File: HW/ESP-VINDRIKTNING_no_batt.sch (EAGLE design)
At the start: 47 parts, among them IC1 PI4ULS5V202UEX, IC3 CH340C, J1 USB-C_DONLY918-418K2022Y40000, Q1 MMDT3904, Q6 DMG2305UX, U1 ESP-12S

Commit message: new
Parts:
- removed D1: 1N5819WS, diode:DIODE-SOD323-R
- removed SLEEP: JUMPER-SMT_2_NO_NO-SILK, LasKKit-Connectors:JUMPER-SMT_2_NO_NO-SILK
- removed U1: ESP-12S, LasKKit-Modules:WIFI_ESP12SMD
- added C6: 100nF, rcl:C-EUC0603
- added C7: 47uF, rcl:C-EUC0603
- added ESP32: ESP32-WROOM-32D, LasKKit-Modules:ESP32-WROOM-32D
- added Q2, Q3, Q4, Q5: AO3404A, SparkFun-DiscreteSemi:MOSFET-NCH-AO3404A
- added R10, R7: 100k, rcl:R-EU_R0402
- added R6: 10k, rcl:R-EU_R0402
- C1: value 100nF -> 20p; device rcl:C-EUC0603 -> rcl:C-EUC0402
- C2: value 10uF -> 20p; device rcl:C-EUC0603 -> rcl:C-EUC0402
- I2C: value JST-XH-4 -> JST-PH-4; device LasKKit-Connectors:JST-XH-4 -> LasKKit-Connectors:JST-PH-4; LCSC_PART (none) -> C2321
- Q6: value DMG2305UX -> 12MHz; device transistor-power:FDN360P -> crystal-geyer_V1_0:KX-7; LCSC_PART C144153 -> C97242
- R3: value 4k7 -> 100k
- R5: value 2k7 -> 10k
- R8: value 470 -> 100k
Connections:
- removed net ADC: U1.ADC
- removed net CH_PD: R2.2, U1.CH_PD
- removed net GPIO0: Q1_1.C, R4.2, U1.GPIO0
- removed net GPIO12: U1.GPIO12, YELLOW1.A, YELLOW2.A
- removed net GPIO13: RED1.A, RED2.A, U1.GPIO13
- removed net GPIO14: GREEN1.A, GREEN2.A, U1.GPIO14
- removed net GPIO15: R5.1, U1.GPIO15
- removed net GPIO16: R8.2, U1.GPIO16
- removed net GPIO2: Q6.G, R3.2, U1.GPIO2
- removed net GPIO4: I2C.4, R12.1, U1.GPIO4
- removed net GPIO5: I2C.3, R13.1, U1.GPIO5
- removed net RST: C5.2, Q1_2.C, R1.2, RESET.3, SLEEP.1, U1.RESET
- removed net RX: IC1.B1, R18.1, U1.RX
- removed net TX: IC1.B2, R19.1, U1.TX
- new net EN: C5.2, ESP32.EN, Q1_2.C, R1.2, RESET.3
- new net IO0: ESP32.IO0, Q1_1.C
- new net IO12: ESP32.IO12, R2.2
- new net IO13: ESP32.IO13
- new net IO14: ESP32.IO14
- new net IO15: ESP32.IO15
- new net IO16: ESP32.IO16, IC1.B1
- new net IO17: ESP32.IO17, IC1.B2
- new net IO18: ESP32.IO18
- new net IO19: ESP32.IO19
- new net IO2: ESP32.IO2
- new net IO21: ESP32.IO21, I2C.4, R12.1
- new net IO22: ESP32.IO22, I2C.3, R13.1
- new net IO23: ESP32.IO23
- new net IO25: ESP32.IO25, R4.1
- new net IO26: ESP32.IO26, R5.1
- new net IO27: ESP32.IO27, R6.1
- new net IO32: ESP32.IO32
- new net IO33: ESP32.IO33
- new net IO34: ESP32.IO34
- new net IO35: ESP32.IO35
- new net IO4: ESP32.IO4
- new net IO5: ESP32.IO5
- new net N$10: Q4.G, R5.2, R8.2
- new net N$17: Q3.G, R4.2, R7.2
- new net N$2: D3.A, FAN.2, Q2.D
- new net N$3: Q2.G, R2.1, R3.1
- new net N$4: C1.2, IC3.XI, Q6.2
- new net N$5: Q5.D, R15.2, R22.2
- new net N$7: Q3.D, R17.2, R20.2
- new net N$9: Q5.G, R10.2, R6.2
- new net RXD0: ESP32.RXD0, R18.1
- new net SENSOR_VN: ESP32.SENSOR_VN
- new net SENSOR_VP: ESP32.SENSOR_VP
- new net TXD0: ESP32.TXD0, R19.1
- net +3V3: now also C6.1, C7.1, ESP32.3V3, GREEN1.A, GREEN2.A, RED1.A, RED2.A, YELLOW1.A, YELLOW2.A; no longer C1.1, C2.1, R2.1, R3.1, R4.1, U1.VCC
- net +5V: now also D3.C, FAN.1; no longer D1.C, Q6.S
- net GND: now also C1.1, C2.1, C6.2, C7.2, ESP32.GND1, ESP32.GND2, ESP32.GND3, ESP32.P_GND, Q2.S, Q3.S, Q4.S, Q5.S, R10.1, R3.2, R7.1, R8.1; no longer C1.2, C2.2, D3.A, FAN.2, R15.2, R16.1, R17.2, R20.2, R21.1, R22.2, R5.2, U1.GND
- net N$18: now also C2.2, IC3.XO, Q6.1; no longer D1.A, D3.C, FAN.1, Q6.D
- net N$6: now also Q4.D, R16.1, R21.1; no longer R8.1, SLEEP.2
- net RX_: now also SENSOR.2; no longer SENSOR.1
- net TX_: now also SENSOR.1; no longer SENSOR.2
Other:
- moved on the sheet: C1, C10, C15, C17, C2, C3, C4, C5, C9, GREEN1, GREEN2, IC1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

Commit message: first working
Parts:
- R12, R13, R15, R16, R17, R20, R21, R22: device rcl:R-EU_R0402 -> rcl:R-EU_R0603
- R18, R19: device rcl:R-EU_R0603 -> rcl:R-EU_R0402
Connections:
- net IO16 renamed RX2
- net IO17 renamed TX2
- net N$5 renamed R
- net N$6 renamed Y
- net N$7 renamed G
- removed net RX_: IC1.A1, SENSOR.2
- removed net TX_: IC1.A2, SENSOR.1
- new net RX: IC1.A2, SENSOR.2
- new net TX: IC1.A1, SENSOR.1
- net +3V3: now also I2C.3; no longer I2C.2
- net GND: now also I2C.4; no longer I2C.1
- net IO21: now also I2C.1; no longer I2C.4
- net IO22: now also I2C.2; no longer I2C.3
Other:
- moved on the sheet: I2C

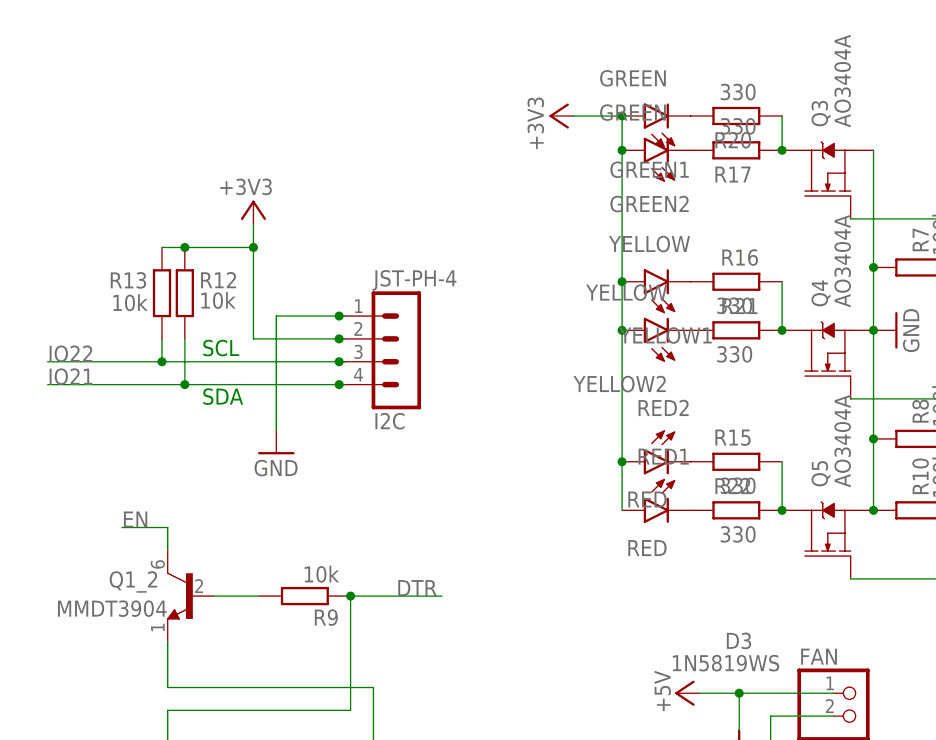
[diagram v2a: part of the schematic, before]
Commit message: connectors pos
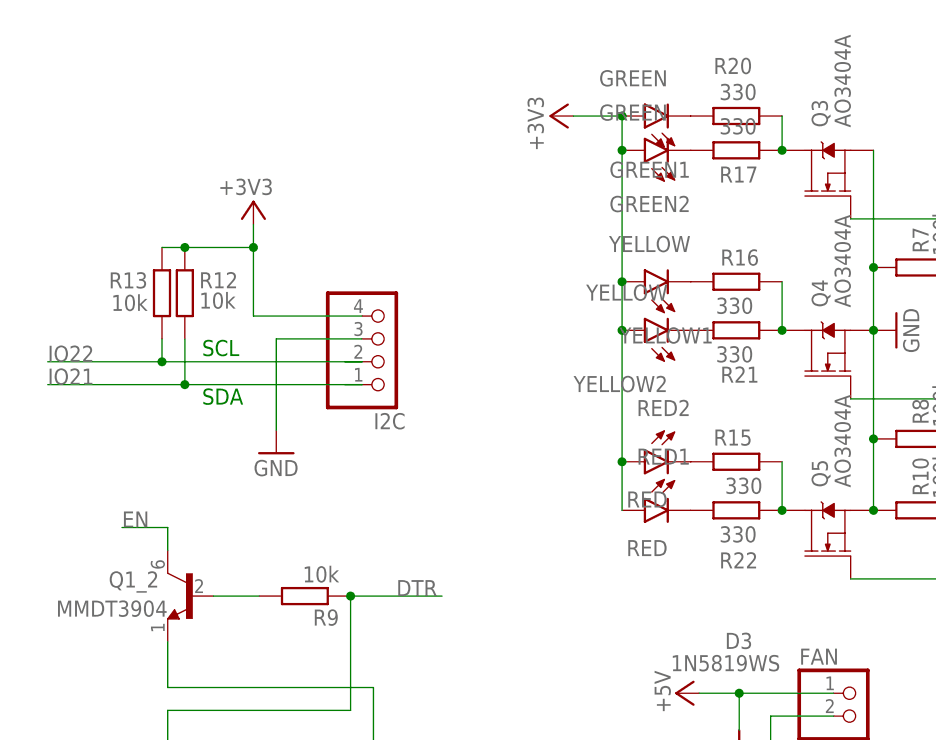
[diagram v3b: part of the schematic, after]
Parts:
- I2C: value JST-PH-4 -> (none); device LasKKit-Connectors:JST-PH-4 -> LasKKit-Connectors:PINHD-1X4
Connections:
- net +3V3: now also I2C.4; no longer I2C.3
- net GND: now also I2C.3; no longer I2C.4
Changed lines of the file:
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@@
 <setting verticaltext="up"/>
 </settings>
-<grid distance="12.5" unitdist="mil" unit="mil" style="lines" multiple="1" display="no" altdistance="0.01" altunitdist="inch" altunit="inch"/>
+<grid distance="25" unitdist="mil" unit="mil" style="lines" multiple="1" display="no" altdistance="0.01" altunitdist="inch" altunit="inch"/>
 <layers>
 <layer number="1" name="Top" color="4" fill="1" visible="no" active="no"/>
@@
 <part name="C2" library="rcl" library_urn="urn:adsk.eagle:library:334" deviceset="C-EU" device="C0402" package3d_urn="urn:adsk.eagle:package:23626/2" value="20p"/>
 <part name="GND6" library="supply1" library_urn="urn:adsk.eagle:library:371" deviceset="GND" device=""/>
-<part name="I2C" library="LasKKit-Connectors" library_urn="urn:adsk.eagle:library:21740355" deviceset="JST-PH-4" device="" package3d_urn="urn:adsk.eagle:package:21740529/2">
+<part name="I2C" library="LasKKit-Connectors" library_urn="urn:adsk.eagle:library:21740355" deviceset="PINHD-1X4" device="" package3d_urn="urn:adsk.eagle:package:21740534/1">
 <attribute name="LCSC_PART" value="C2321"/>
 </part>
@@
 <instance part="R15" gate="G$1" x="220.6625" y="129.2225" smashed="yes" rot="MR180">
 <attribute name="NAME" x="218.1225" y="132.8039" size="1.778" layer="95" rot="MR180"/>
-<attribute name="VALUE" x="218.7575" y="127.4445" size="1.778" layer="96" rot="MR180"/>
+<attribute name="VALUE" x="219.3925" y="127.4445" size="1.778" layer="96" rot="MR180"/>
 </instance>
 <instance part="R16" gate="G$1" x="220.6625" y="149.225" smashed="yes" rot="R180">
@@
 </instance>
 <instance part="R17" gate="G$1" x="220.6625" y="163.83" smashed="yes">
-<attribute name="NAME" x="218.1225" y="160.2486" size="1.778" layer="95"/>
+<attribute name="NAME" x="218.7575" y="160.2486" size="1.778" layer="95"/>
 <attribute name="VALUE" x="218.7575" y="165.608" size="1.778" layer="96"/>
 </instance>
@@
 </instance>
 <instance part="R20" gate="G$1" x="220.6625" y="167.64" smashed="yes">
-<attribute name="NAME" x="218.1225" y="164.0586" size="1.778" layer="95"/>
+<attribute name="NAME" x="218.1225" y="172.3136" size="1.778" layer="95"/>
 <attribute name="VALUE" x="218.7575" y="169.418" size="1.778" layer="96"/>
 </instance>
 <instance part="R21" gate="G$1" x="220.6625" y="143.8275" smashed="yes" rot="R180">
-<attribute name="NAME" x="223.2025" y="147.4089" size="1.778" layer="95" rot="R180"/>
+<attribute name="NAME" x="223.2025" y="139.7889" size="1.778" layer="95" rot="R180"/>
 <attribute name="VALUE" x="222.5675" y="142.0495" size="1.778" layer="96" rot="R180"/>
 </instance>
 <instance part="R22" gate="G$1" x="220.6625" y="123.825" smashed="yes" rot="MR180">
-<attribute name="NAME" x="218.1225" y="127.4064" size="1.778" layer="95" rot="MR180"/>
+<attribute name="NAME" x="218.7575" y="119.1514" size="1.778" layer="95" rot="MR180"/>
 <attribute name="VALUE" x="218.7575" y="122.047" size="1.778" layer="96" rot="MR180"/>
 </instance>
@@
 <attribute name="VALUE" x="71.12" y="4.7625" size="1.778" layer="96"/>
 </instance>
-<instance part="I2C" gate="G$1" x="181.61" y="142.875" smashed="yes" rot="MR180">
+<instance part="I2C" gate="A" x="181.61" y="142.875" smashed="yes" rot="MR180">
 <attribute name="NAME" x="180.34" y="134.62" size="1.778" layer="95" rot="MR180"/>
 <attribute name="VALUE" x="180.34" y="150.495" size="1.778" layer="95" rot="MR180"/>
@@
 <segment>
 <pinref part="GND11" gate="1" pin="GND"/>
-<wire x1="169.545" y1="132.715" x2="169.545" y2="145.415" width="0.1524" layer="91"/>
-<wire x1="177.165" y1="145.415" x2="176.53" y2="145.415" width="0.1524" layer="91"/>
-<pinref part="I2C" gate="G$1" pin="4"/>
-<wire x1="176.53" y1="145.415" x2="169.545" y2="145.415" width="0.1524" layer="91"/>
-<junction x="176.53" y="145.415"/>
+<wire x1="169.545" y1="132.715" x2="169.545" y2="142.875" width="0.1524" layer="91"/>
+<pinref part="I2C" gate="A" pin="3"/>
+<wire x1="179.07" y1="142.875" x2="169.545" y2="142.875" width="0.1524" layer="91"/>
 </segment>
 <segment>
@@
 <pinref part="R13" gate="G$1" pin="2"/>
 <pinref part="R12" gate="G$1" pin="2"/>
-<wire x1="167.005" y1="153.035" x2="167.005" y2="142.875" width="0.1524" layer="91"/>
+<wire x1="167.005" y1="153.035" x2="167.005" y2="145.415" width="0.1524" layer="91"/>
 <wire x1="156.845" y1="153.035" x2="159.385" y2="153.035" width="0.1524" layer="91"/>
 <wire x1="159.385" y1="153.035" x2="167.005" y2="153.035" width="0.1524" layer="91"/>
 <junction x="159.385" y="153.035"/>
 <junction x="167.005" y="153.035"/>
-<wire x1="177.165" y1="142.875" x2="176.53" y2="142.875" width="0.1524" layer="91"/>
-<pinref part="I2C" gate="G$1" pin="3"/>
-<wire x1="176.53" y1="142.875" x2="167.005" y2="142.875" width="0.1524" layer="91"/>
-<junction x="176.53" y="142.875"/>
+<pinref part="I2C" gate="A" pin="4"/>
+<wire x1="179.07" y1="145.415" x2="167.005" y2="145.415" width="0.1524" layer="91"/>
 </segment>
 <segment>
@@
 <wire x1="156.845" y1="140.335" x2="144.145" y2="140.335" width="0.1524" layer="91"/>
 <wire x1="156.845" y1="142.875" x2="156.845" y2="140.335" width="0.1524" layer="91"/>
-<wire x1="177.165" y1="140.335" x2="176.53" y2="140.335" width="0.1524" layer="91"/>
+<wire x1="177.165" y1="140.335" x2="179.07" y2="140.335" width="0.1524" layer="91"/>
 <junction x="156.845" y="140.335"/>
-<pinref part="I2C" gate="G$1" pin="2"/>
-<wire x1="176.53" y1="140.335" x2="156.845" y2="140.335" width="0.1524" layer="91"/>
-<junction x="176.53" y="140.335"/>
+<pinref part="I2C" gate="A" pin="2"/>
+<wire x1="179.07" y1="140.335" x2="156.845" y2="140.335" width="0.1524" layer="91"/>
 </segment>
 </net>
@@
 <wire x1="159.385" y1="137.795" x2="144.145" y2="137.795" width="0.1524" layer="91"/>
 <wire x1="159.385" y1="142.875" x2="159.385" y2="137.795" width="0.1524" layer="91"/>
-<wire x1="177.165" y1="137.795" x2="176.53" y2="137.795" width="0.1524" layer="91"/>
+<wire x1="177.165" y1="137.795" x2="179.07" y2="137.795" width="0.1524" layer="91"/>
 <junction x="159.385" y="137.795"/>
-<pinref part="I2C" gate="G$1" pin="1"/>
-<wire x1="176.53" y1="137.795" x2="159.385" y2="137.795" width="0.1524" layer="91"/>
-<junction x="176.53" y="137.795"/>
-</segment>
-</net>
+<pinref part="I2C" gate="A" pin="1"/>
+<wire x1="179.07" y1="137.795" x2="159.385" y2="137.795" width="0.1524" layer="91"/>
+</segment>
+</net>
